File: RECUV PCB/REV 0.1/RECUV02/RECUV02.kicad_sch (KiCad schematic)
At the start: 7 parts, among them U1 ESP32-S3-WROOM-1, U2 CH340C

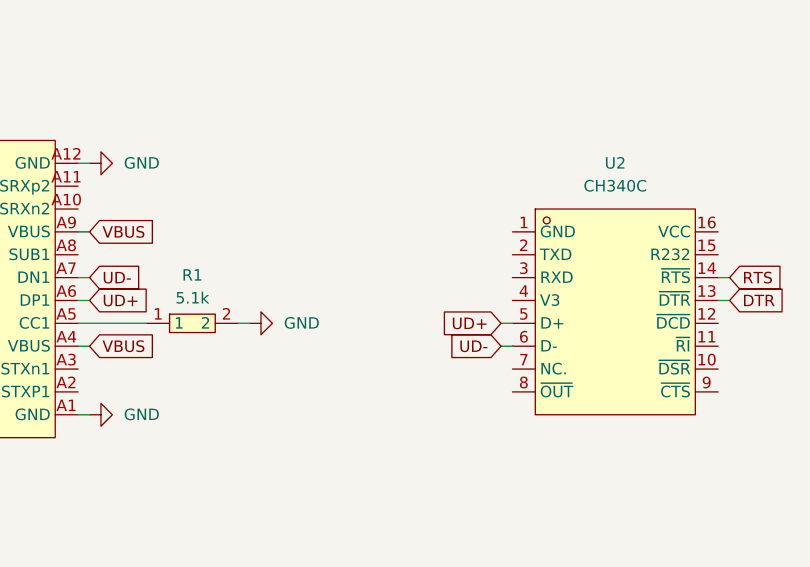
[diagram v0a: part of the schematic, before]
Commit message: Added V3 and GND to CH340
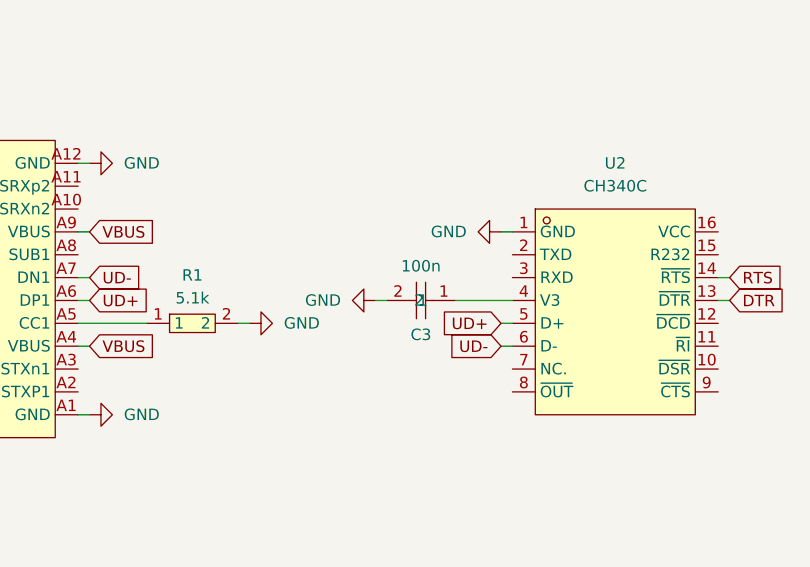
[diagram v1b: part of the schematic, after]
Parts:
- added C3: 100n, EasyEDA:C0805, symbol EasyEDA:CL21B104KBCNNNC
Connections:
- net GND: now also U2.1 (GND), C3.2
- net at U2.4 (V3): now also C3.1

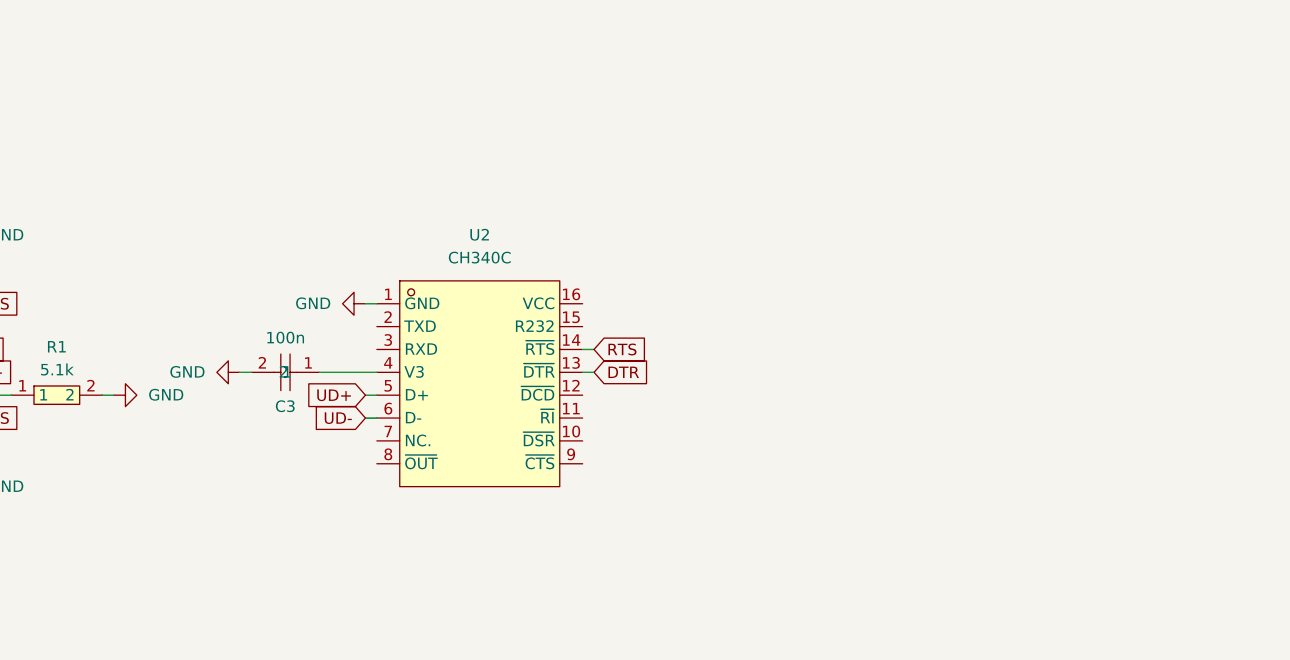
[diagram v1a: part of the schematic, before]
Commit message: Added LED, TX and RX to CH340
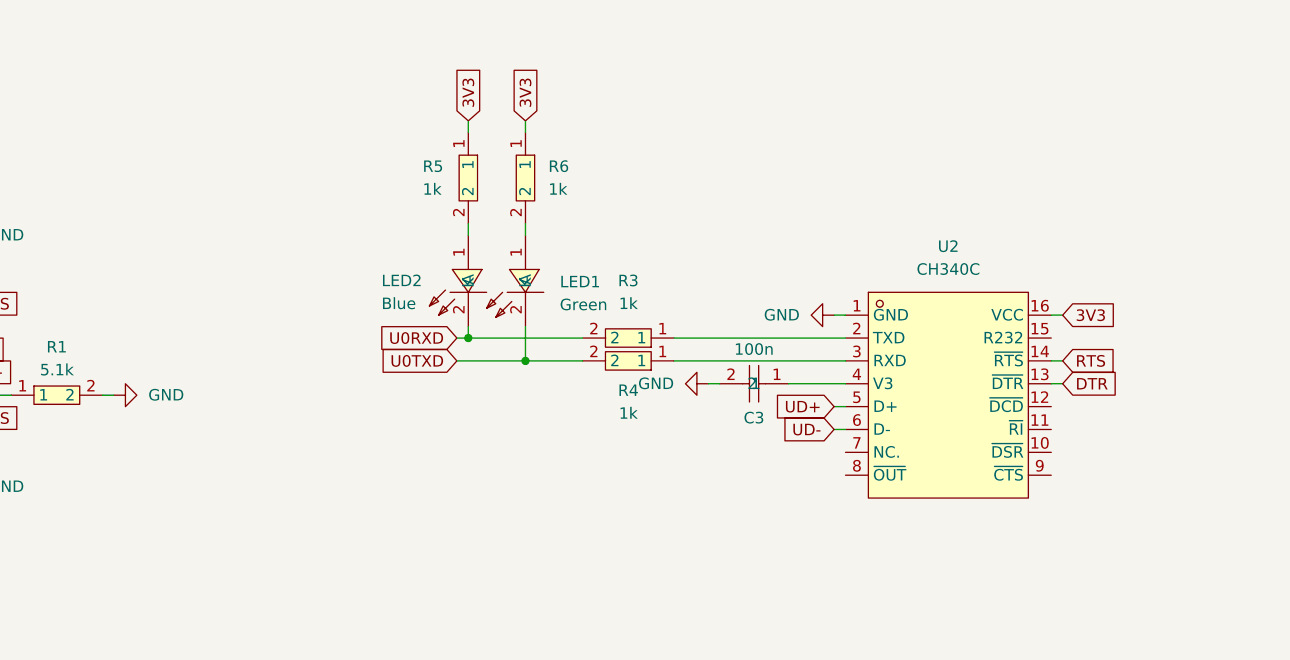
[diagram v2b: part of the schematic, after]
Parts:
- added LED1: Green, EasyEDA:LED0805-R-RD, symbol EasyEDA:0805G
- added LED2: Blue, EasyEDA:LED0805-R-RD, symbol EasyEDA:XL-0805QBC
- added R3, R4, R5, R6: 1k, EasyEDA:R0805, symbol EasyEDA:0805W8F1001T5E
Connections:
- net 3V3: now reaches U2.16 (VCC)
- net 3V3: now also R5.1, R6.1
- net at U2.2 (TXD): now also R3.1
- net at U2.3 (RXD): now also R4.1
- new net: LED1.1 (A), R6.2
- new net: LED2.1 (A), R5.2
- new net U0RXD: LED2.2 (K), R3.2
- new net U0TXD: LED1.2 (K), R4.2
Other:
- moved on the sheet: C3, U2

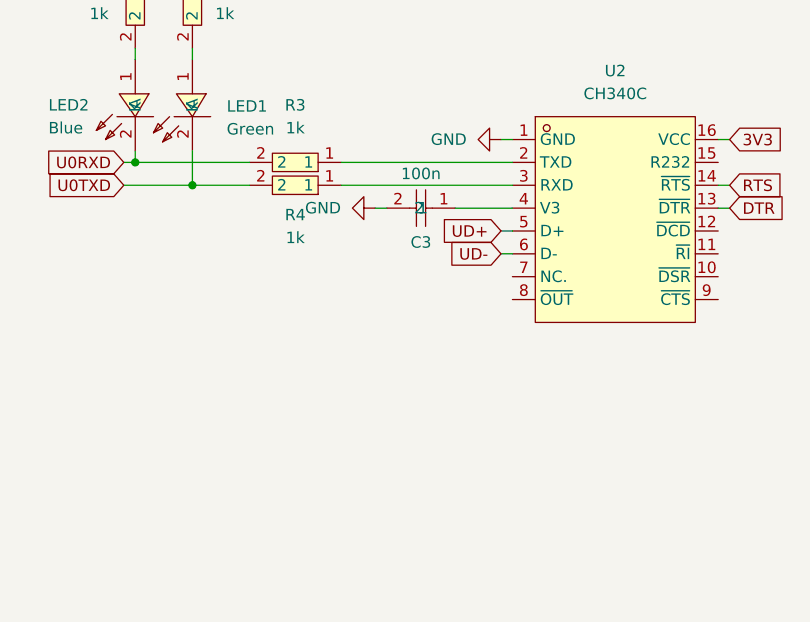
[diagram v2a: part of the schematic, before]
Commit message: Corrected V3 PIN for CH340
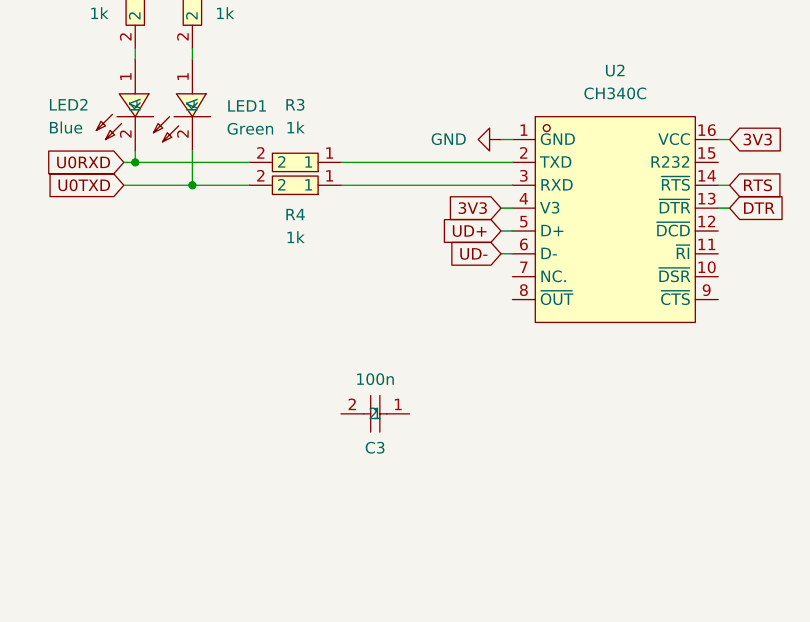
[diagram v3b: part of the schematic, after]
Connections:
- net 3V3: now also U2.4 (V3)
- net GND: no longer C3.2
- net at C3.1: no longer U2.4 (V3)
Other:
- moved on the sheet: C3
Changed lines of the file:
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@@
 	(wire
 		(pts
-			(xy 162.56 53.34) (xy 168.91 53.34)
+			(xy 31.75 83.82) (xy 31.75 85.09)
 		)
 		(stroke
@@
 	(wire
 		(pts
-			(xy 31.75 83.82) (xy 31.75 85.09)
+			(xy 68.58 44.45) (xy 69.85 44.45)
 		)
 		(stroke
@@
 	(wire
 		(pts
-			(xy 68.58 44.45) (xy 69.85 44.45)
+			(xy 68.58 57.15) (xy 69.85 57.15)
 		)
 		(stroke
@@
 	(wire
 		(pts
-			(xy 68.58 57.15) (xy 69.85 57.15)
+			(xy 167.64 53.34) (xy 168.91 53.34)
 		)
 		(stroke
@@
 	(wire
 		(pts
-			(xy 153.67 53.34) (xy 154.94 53.34)
-		)
-		(stroke
-			(width 0)
-			(type default)
-		)
-	)
-	(wire
-		(pts
 			(xy 68.58 49.53) (xy 69.85 49.53)
 		)
@@
 		)
 	)
+	(global_label "3V3"
+		(shape input)
+		(at 167.64 53.34 180)
+		(fields_autoplaced yes)
+		(effects
+			(font
+				(size 1.27 1.27)
+			)
+			(justify right)
+		)
+		(property "Intersheetrefs" "${INTERSHEET_REFS}"
+			(at 161.1472 53.34 0)
+			(hide yes)
+			(show_name no)
+			(do_not_autoplace no)
+			(effects
+				(font
+					(size 1.27 1.27)
+				)
+				(justify right)
+			)
+		)
+	)
 	(global_label "UD-"
 		(shape input)
@@
 	(symbol
 		(lib_id "EasyEDA:CL21B104KBCNNNC")
-		(at 158.75 53.34 180)
+		(at 153.67 76.2 180)
 		(unit 1)
 		(body_style 1)
@@
 		(dnp no)
 		(property "Reference" "C3"
-			(at 158.75 57.15 0)
+			(at 153.67 80.01 0)
 			(show_name no)
 			(do_not_autoplace no)
@@
 		)
 		(property "Value" "100n"
-			(at 158.75 49.53 0)
+			(at 153.67 72.39 0)
 			(show_name no)
 			(do_not_autoplace no)
@@
 		)
 		(property "Footprint" "EasyEDA:C0805"
-			(at 158.75 45.72 0)
+			(at 153.67 68.58 0)
 			(hide yes)
 			(show_name no)
@@
 		)
 		(property "Datasheet" "https://lcsc.com/product-detail/Multilayer-Ceramic-Capacitors-MLCC-SMD-SMT_SAMSUNG_CL21B104KBCNNNC_100nF-104-10-50V_C1711.html"
-			(at 158.75 43.18 0)
+			(at 153.67 66.04 0)
 			(hide yes)
 			(show_name no)
@@
 		)
 		(property "Description" "100nF (104) ±10% 50V"
-			(at 158.75 53.34 0)
+			(at 153.67 76.2 0)
 			(hide yes)
 			(show_name no)
@@
 		)
 		(property "Manufacturer" "SAMSUNG(三星)"
-			(at 158.75 40.64 0)
+			(at 153.67 63.5 0)
 			(hide yes)
 			(show_name no)
@@
 		)
 		(property "MPN" "CL21B104KBCNNNC"
-			(at 158.75 38.1 0)
+			(at 153.67 60.96 0)
 			(hide yes)
 			(show_name no)
@@
 		)
 		(property "LCSC Part" "C1711"
-			(at 158.75 35.56 0)
+			(at 153.67 58.42 0)
 			(hide yes)
 			(show_name no)
@@
 					(unit 1)
 				)
-			)
-		)
-	)
-	(symbol
-		(lib_id "power:GND")
-		(at 153.67 53.34 270)
-		(unit 1)
-		(body_style 1)
-		(exclude_from_sim no)
-		(in_bom yes)
-		(on_board yes)
-		(in_pos_files yes)
-		(dnp no)
-		(fields_autoplaced yes)
-		(property "Reference" "#PWR010"
-			(at 147.32 53.34 0)
-			(hide yes)
-			(show_name no)
-			(do_not_autoplace no)
-			(effects
-				(font
-					(size 1.27 1.27)
-				)
-			)
-		)
-		(property "Value" "GND"
-			(at 149.86 53.3399 90)
-			(show_name no)
-			(do_not_autoplace no)
-			(effects
-				(font
-					(size 1.27 1.27)
-				)
-				(justify right)
-			)
-		)
-		(property "Footprint" ""
-			(at 153.67 53.34 0)
-			(hide yes)
-			(show_name no)
-			(do_not_autoplace no)
-			(effects
-				(font
-					(size 1.27 1.27)
-				)
-			)
-		)
-		(property "Datasheet" ""
-			(at 153.67 53.34 0)
-			(hide yes)
-			(show_name no)
-			(do_not_autoplace no)
-			(effects
-				(font
-					(size 1.27 1.27)
-				)
-			)
-		)
-		(property "Description" "Power symbol creates a global label with name \"GND\" , ground"
-			(at 153.67 53.34 0)
-			(hide yes)
-			(show_name no)
-			(do_not_autoplace no)
-			(effects
-				(font
-					(size 1.27 1.27)
-				)
-			)
-		)
-		(pin "1"
-		)
-		(instances
-			(project "RECUV02"
-				(path "/2b6cdc4d-a2c2-48c0-8972-6d5f3f53de15"
-					(reference "#PWR010")
-					(unit 1)
-				)

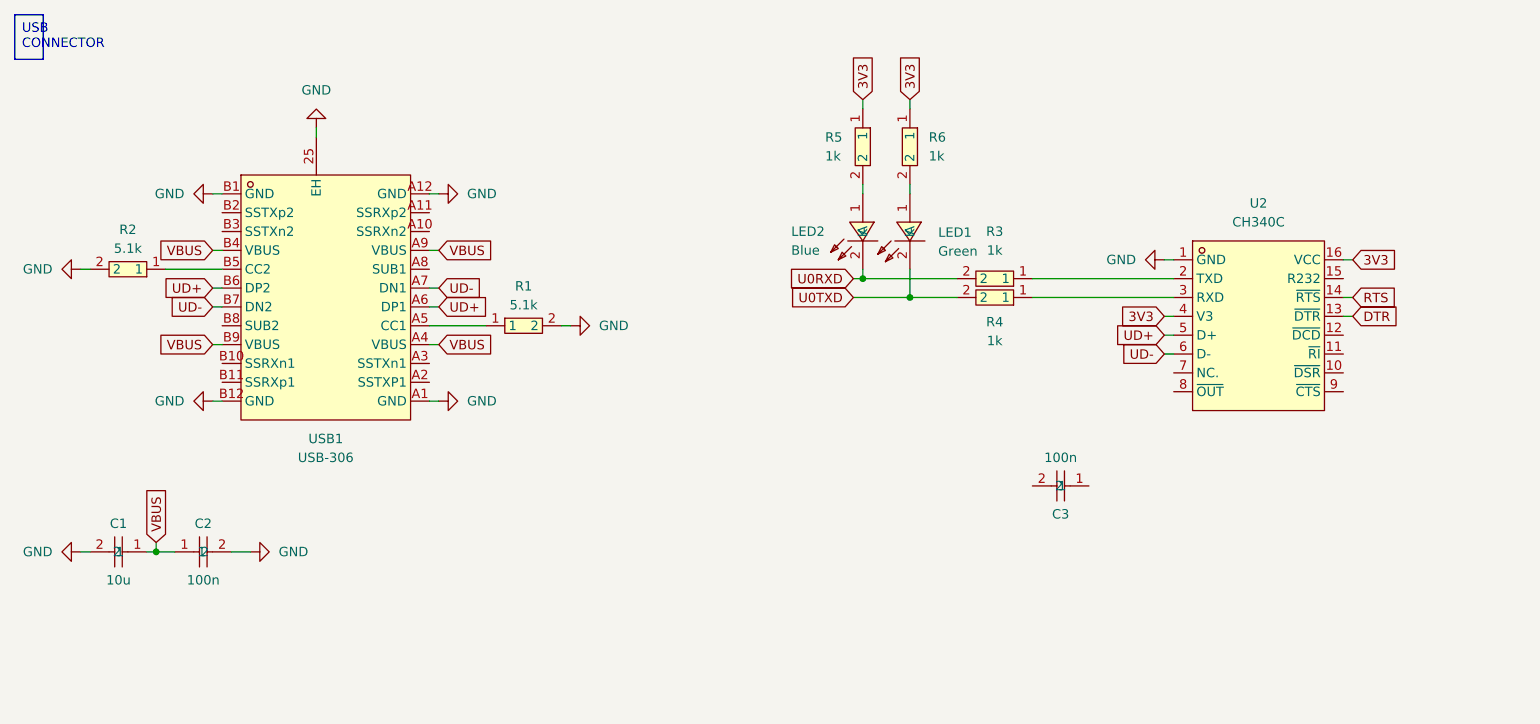
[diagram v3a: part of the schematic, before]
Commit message: Reorganized and changed 1k by 470 for led intensity
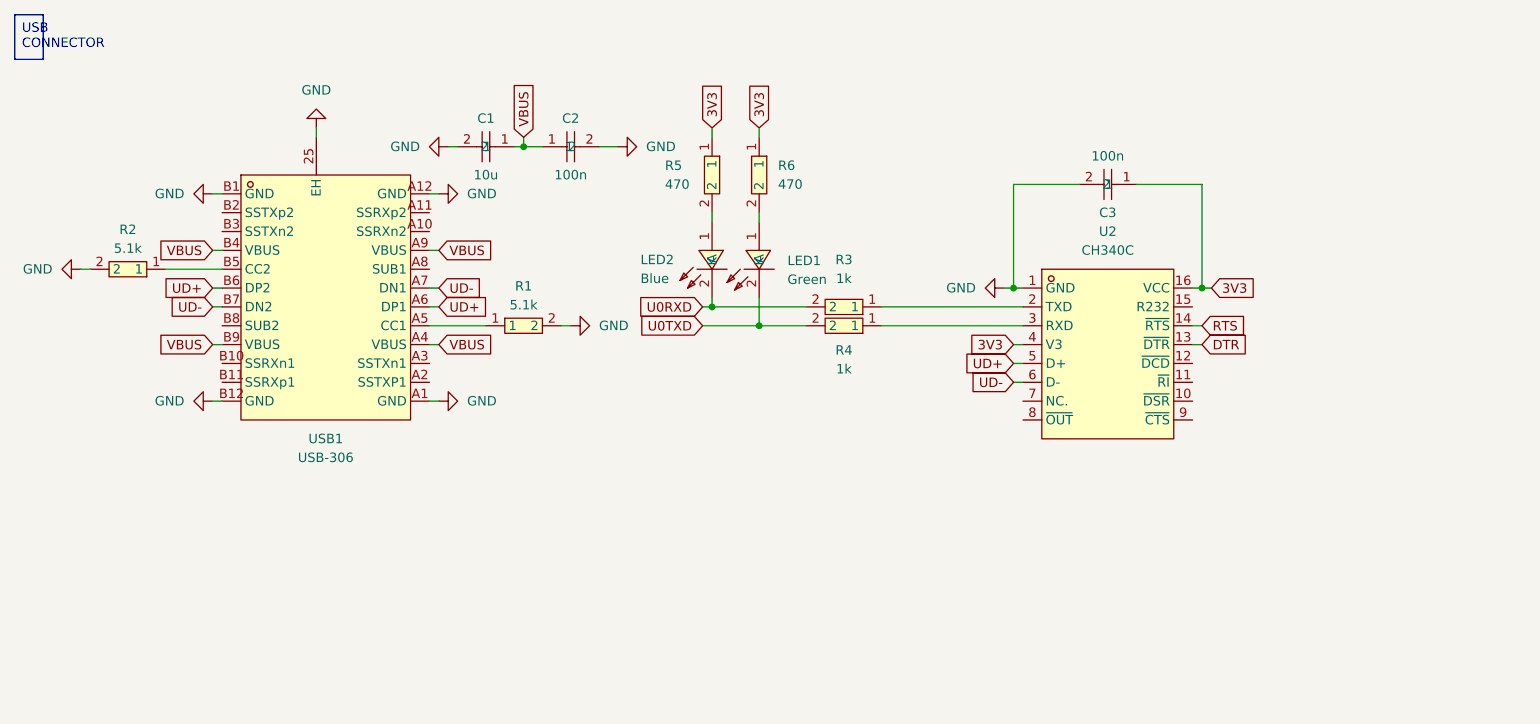
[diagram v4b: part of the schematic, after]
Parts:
- removed R5, R6: 1k, EasyEDA:R0805, symbol EasyEDA:0805W8F1001T5E
- added R5, R6: 470, EasyEDA:R0805, symbol EasyEDA:0805W8F4700T5E
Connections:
- net 3V3: now also C3.1, R5.1, R6.1
- net GND: now also C3.2
- net at LED1.1 (A): now also R6.2
- net at LED2.1 (A): now also R5.2
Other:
- moved on the sheet: C1, C2, C3, LED1, LED2, R3, R4, U2
